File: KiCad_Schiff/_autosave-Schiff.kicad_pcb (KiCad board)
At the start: 2 copper layers, 150 x 60 mm, 28 parts, among them J1 Conn_01x02, J2 L298N, J3 AMS1117-Module, J4 L298N, J5 Screw_Terminal_01x02, J6 Screw_Terminal_01x02, M1 Motor_Servo, M2 Motor_Servo, M3 Motor_Servo, SW1 SW_Wuerth_450301014042, SW2 SW_Wuerth_450301014042, U1 NRF24L01_Breakout

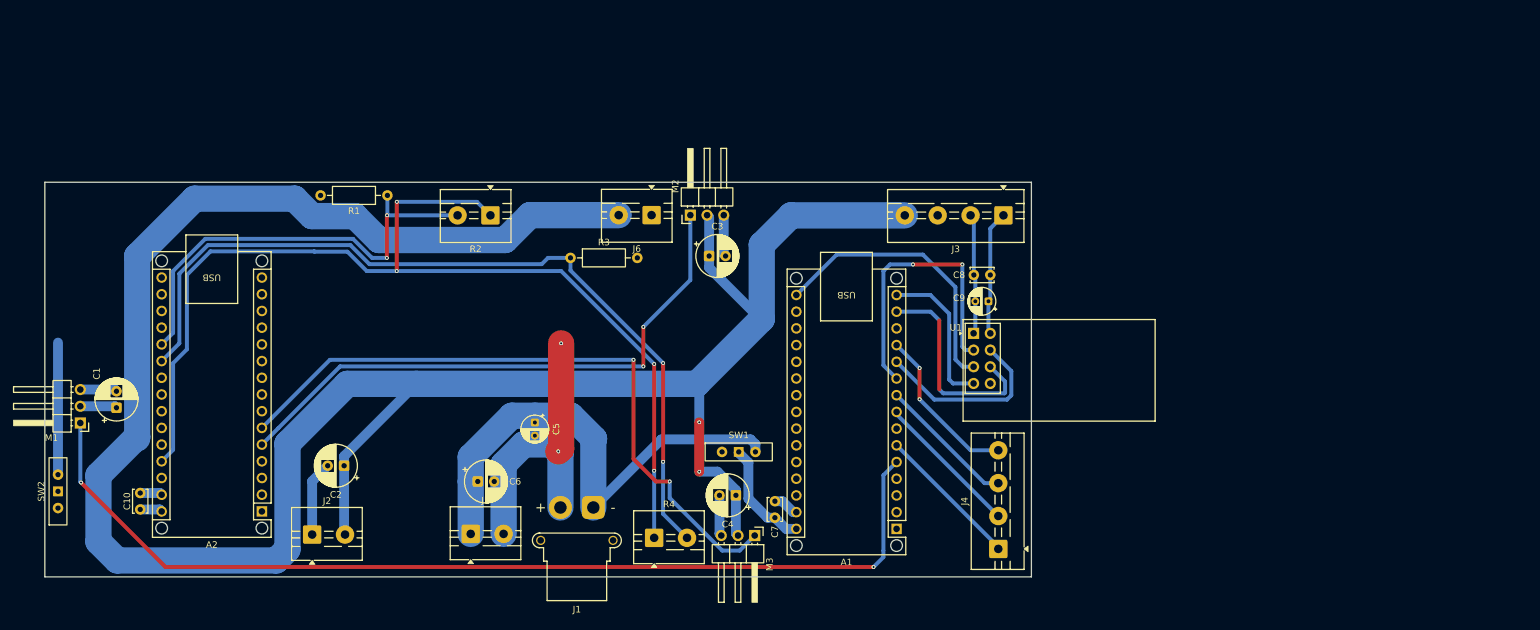
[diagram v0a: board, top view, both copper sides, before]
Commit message: Changed footprints
Changed footprints to match the given bore sizes
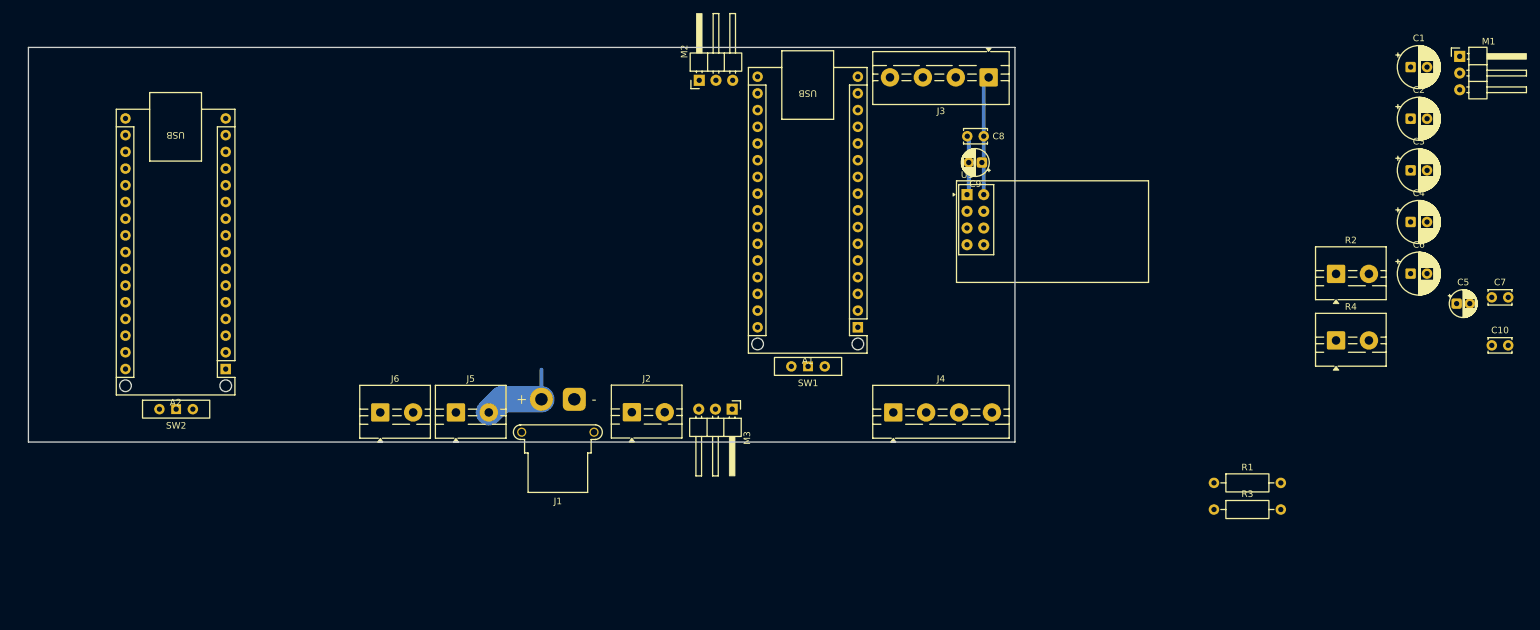
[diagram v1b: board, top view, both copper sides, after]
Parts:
- A1, A2: footprint Module:Arduino_Nano_WithMountingHoles -> LibraryNewHoleSize:Arduino_Nano_WithMountingHoles
- C5, C9: footprint Capacitor_THT:CP_Radial_D4.0mm_P2.00mm -> LibraryNewHoleSize:CP_Radial_D4.0mm_P2.00mm
- M1, M2, M3: footprint Connector_PinHeader_2.54mm:PinHeader_1x03_P2.54mm_Horizontal -> LibraryNewHoleSize:PinHeader_1x03_P2.54mm_Horizontal
- U1: footprint RF_Module:nRF24L01_Breakout -> LibraryNewHoleSize:nRF24L01_Breakout
- moved M1 217.0 mm to (235.6, 19.4), turned to 0 degrees
- moved C10 206.7 mm to (240.5, 63.3), turned to 0 degrees
- moved C1 203.5 mm to (228.2, 21.0), turned to 0 degrees
- moved C2 170.5 mm to (228.2, 28.8), turned to 0 degrees
- moved C6 145.3 mm to (228.2, 52.4)
- moved C5 141.3 mm to (235.2, 57.0), turned to 0 degrees
- moved R1 133.1 mm to (198.3, 84.2), turned to 0 degrees
- moved R2 128.9 mm to (216.8, 52.4), turned to 0 degrees
- moved C7 113.3 mm to (240.5, 56.0), turned to 0 degrees
- moved C4 110.7 mm to (228.2, 44.5), turned to 0 degrees
- moved R4 107.9 mm to (216.8, 62.5)
- moved C3 107.4 mm to (228.2, 36.7)
- moved R3 105.1 mm to (198.3, 88.3)
- moved J2 52.0 mm to (109.8, 73.5)
- moved J6 51.0 mm to (71.5, 73.5), turned to 0 degrees
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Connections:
- J1 pad 1: VCC_BT -> GND
- J1 pad 2: GND -> VCC_BT
- J5 pad 1: VCC_BT -> GND
- J5 pad 2: GND -> VCC_BT
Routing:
- net +5V: track 368.5 -> 0.00 mm, vias 2 -> 0
- net Net-(A2-+5V): track 161.6 -> 0.00 mm, vias 4 -> 0
- net /ServoStear: track 152.3 -> 0.00 mm, vias 2 -> 0
- net Net-(A2-A2): track 127.2 -> 0.00 mm, vias 2 -> 0
- net /ServoFoilR: track 102.5 -> 0.00 mm, vias 2 -> 0
- net GND: track 104.8 -> 9.08 mm, vias 2 -> 0
- net /ServoFoilL: track 88.9 -> 0.00 mm, vias 2 -> 0
- net VCC_BT: track 97.6 -> 13.3 mm
- net Net-(A2-A1): track 67.9 -> 0.00 mm, vias 2 -> 0
- net Net-(A1-D7): track 44.0 -> 0.00 mm, vias 2 -> 0
- net Net-(A1-D13): track 43.0 -> 0.00 mm
- net Net-(A1-D11): track 32.7 -> 0.00 mm
- net Net-(A1-D8): track 28.3 -> 0.00 mm
- net /IN4: track 24.9 -> 0.00 mm, vias 2 -> 0
- net Net-(A1-D12): track 23.1 -> 0.00 mm
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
